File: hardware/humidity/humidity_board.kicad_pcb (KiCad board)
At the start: 2 copper layers, 21 parts, among them IC1 ATMEGA88-A, J1 RJ45, P1 ISP, P2 UART, SW1 SW_RESET, U1 ST485, U2 HYT271

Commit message: begin with humidity board pcb
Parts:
- moved U2 12.2 mm to (152.0, 149.0)
- moved J1 0.56 mm to (262.0, 149.0)
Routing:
- net GND: track 0.00 -> 29.6 mm
- net VCC: track 0.00 -> 3.14 mm
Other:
- net class Default: trace_width 0.254 -> 0.7; via_dia 0.889 -> 1.2; via_drill 0.635 -> 0.6
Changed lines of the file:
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@@
   (general
     (links 61)
-    (no_connects 61)
-    (area 0 0 0 0)
+    (no_connects 57)
+    (area 159.572 124.481 284.2884 167.38335)
     (thickness 1.6)
-    (drawings 0)
-    (tracks 0)
+    (drawings 1)
+    (tracks 11)
     (zones 0)
     (modules 21)
@@
   )
   (setup
-    (last_trace_width 0.254)
+    (last_trace_width 0.7)
     (trace_clearance 0.254)
     (zone_clearance 0.508)
@@
     (segment_width 0.2)
     (edge_width 0.1)
-    (via_size 0.889)
-    (via_drill 0.635)
+    (via_size 1.2)
+    (via_drill 0.6)
     (via_min_size 0.889)
     (via_min_drill 0.508)
@@
     (pad_to_mask_clearance 0)
     (aux_axis_origin 0 0)
-    (visible_elements FFFFFBBF)
+    (visible_elements FFFFFFBF)
     (pcbplotparams
       (layerselection 3178497)
@@
   (net_class Default "This is the default net class."
     (clearance 0.254)
-    (trace_width 0.254)
-    (via_dia 0.889)
-    (via_drill 0.635)
+    (trace_width 0.7)
+    (via_dia 1.2)
+    (via_drill 0.6)
     (uvia_dia 0.508)
     (uvia_drill 0.127)
@@
     (add_net VCC)
   )
+  (module RJ45_8P8_simple (layer F.Cu)
+    (at 262 149 270)
+    (tags RJ45)
+    (fp_text reference J1 (at 0 -21.5 270) (layer F.SilkS)
+      (effects (font (size 1.524 1.524) (thickness 0.3048)))
+    )
+    (fp_text value RJ45 (at 0.14224 -0.1016 270) (layer F.SilkS)
+      (effects (font (size 1.00076 1.00076) (thickness 0.2032)))
+    )
+    (fp_line (start 5.5 -20) (end 5.5 -9) (layer F.SilkS) (width 0.15))
+    (fp_line (start -5.5 -9) (end 5.5 -9) (layer F.SilkS) (width 0.15))
+    (fp_line (start -5.5 -20) (end -5.5 -9) (layer F.SilkS) (width 0.15))
+    (fp_line (start -8 -20) (end 8 -20) (layer F.SilkS) (width 0.15))
+    (fp_line (start 8 -20) (end 8 1.5) (layer F.SilkS) (width 0.15))
+    (fp_line (start 8 1.5) (end -8 1.5) (layer F.SilkS) (width 0.15))
+    (fp_line (start -8 1.5) (end -8 -20) (layer F.SilkS) (width 0.15))
+    (pad "" np_thru_hole circle (at -5.715 -8.9 90) (size 3.4 3.4) (drill 3.4)
+      (layers *.Cu *.SilkS *.Mask)
+    )
+    (pad "" np_thru_hole circle (at 5.715 -8.9 90) (size 3.4 3.4) (drill 3.4)
+      (layers *.Cu *.SilkS *.Mask)
+    )
+    (pad 1 thru_hole rect (at 4.445 -2.54 90) (size 1.9 1.9) (drill 0.8)
+      (layers *.Cu *.Mask F.SilkS)
+      (net 12 /za)
+    )
+    (pad 2 thru_hole circle (at 3.175 0 90) (size 1.9 1.9) (drill 0.8)
+      (layers *.Cu *.Mask F.SilkS)
+      (net 13 /zb)
+    )
+    (pad 3 thru_hole circle (at 1.905 -2.54 90) (size 1.9 1.9) (drill 0.8)
+      (layers *.Cu *.Mask F.SilkS)
+    )
+    (pad 4 thru_hole circle (at 0.63 0 90) (size 1.9 1.9) (drill 0.8)
+      (layers *.Cu *.Mask F.SilkS)
+      (net 18 VCC)
+    )
+    (pad 5 thru_hole circle (at -0.635 -2.54 90) (size 1.9 1.9) (drill 0.8)
+      (layers *.Cu *.Mask F.SilkS)
+      (net 18 VCC)
+    )
+    (pad 6 thru_hole circle (at -1.905 0 90) (size 1.9 1.9) (drill 0.8)
+      (layers *.Cu *.Mask F.SilkS)
+    )
+    (pad 7 thru_hole circle (at -3.175 -2.54 90) (size 1.9 1.9) (drill 0.8)
+      (layers *.Cu *.Mask F.SilkS)
+      (net 14 GND)
+    )
+    (pad 8 thru_hole circle (at -4.445 0 90) (size 1.9 1.9) (drill 0.8)
+      (layers *.Cu *.Mask F.SilkS)
+      (net 14 GND)
+    )
+    (pad 9 thru_hole circle (at 7.9 -12 90) (size 3 3) (drill 1.6)
+      (layers *.Cu *.Mask F.SilkS)
+      (net 14 GND)
+    )
+    (pad 9 thru_hole circle (at -7.9 -12 90) (size 3 3) (drill 1.6)
+      (layers *.Cu *.Mask F.SilkS)
+      (net 14 GND)
+    )
+    (model connectors/RJ45_8.wrl
+      (at (xyz 0 0 0))
+      (scale (xyz 0.4 0.4 0.4))
+      (rotate (xyz 0 0 0))
+    )
+  )
   (module wannenstecker_2x5_rm254 (layer F.Cu)
     (at 220.98 130.81)
@@
     )
   )
-  (module RJ45_8P8_simple (layer F.Cu)
-    (at 261.62 148.59 270)
-    (tags RJ45)
-    (fp_text reference J1 (at 0 -21.5 270) (layer F.SilkS)
-      (effects (font (size 1.524 1.524) (thickness 0.3048)))
-    )
-    (fp_text value RJ45 (at 0.14224 -0.1016 270) (layer F.SilkS)
-      (effects (font (size 1.00076 1.00076) (thickness 0.2032)))
-    )
-    (fp_line (start 5.5 -20) (end 5.5 -9) (layer F.SilkS) (width 0.15))
-    (fp_line (start -5.5 -9) (end 5.5 -9) (layer F.SilkS) (width 0.15))
-    (fp_line (start -5.5 -20) (end -5.5 -9) (layer F.SilkS) (width 0.15))
-    (fp_line (start -8 -20) (end 8 -20) (layer F.SilkS) (width 0.15))
-    (fp_line (start 8 -20) (end 8 1.5) (layer F.SilkS) (width 0.15))
-    (fp_line (start 8 1.5) (end -8 1.5) (layer F.SilkS) (width 0.15))
-    (fp_line (start -8 1.5) (end -8 -20) (layer F.SilkS) (width 0.15))
-    (pad "" np_thru_hole circle (at -5.715 -8.9 90) (size 3.4 3.4) (drill 3.4)
-      (layers *.Cu *.SilkS *.Mask)
-    )
-    (pad "" np_thru_hole circle (at 5.715 -8.9 90) (size 3.4 3.4) (drill 3.4)
-      (layers *.Cu *.SilkS *.Mask)
-    )
-    (pad 1 thru_hole rect (at 4.445 -2.54 90) (size 1.9 1.9) (drill 0.8)
-      (layers *.Cu *.Mask F.SilkS)
-      (net 12 /za)
-    )
-    (pad 2 thru_hole circle (at 3.175 0 90) (size 1.9 1.9) (drill 0.8)
-      (layers *.Cu *.Mask F.SilkS)
-      (net 13 /zb)
-    )
-    (pad 3 thru_hole circle (at 1.905 -2.54 90) (size 1.9 1.9) (drill 0.8)
-      (layers *.Cu *.Mask F.SilkS)
-    )
-    (pad 4 thru_hole circle (at 0.63 0 90) (size 1.9 1.9) (drill 0.8)
-      (layers *.Cu *.Mask F.SilkS)
-      (net 18 VCC)
-    )
-    (pad 5 thru_hole circle (at -0.635 -2.54 90) (size 1.9 1.9) (drill 0.8)
-      (layers *.Cu *.Mask F.SilkS)
-      (net 18 VCC)
-    )
-    (pad 6 thru_hole circle (at -1.905 0 90) (size 1.9 1.9) (drill 0.8)
-      (layers *.Cu *.Mask F.SilkS)
-    )
-    (pad 7 thru_hole circle (at -3.175 -2.54 90) (size 1.9 1.9) (drill 0.8)
-      (layers *.Cu *.Mask F.SilkS)
-      (net 14 GND)
-    )
-    (pad 8 thru_hole circle (at -4.445 0 90) (size 1.9 1.9) (drill 0.8)
-      (layers *.Cu *.Mask F.SilkS)
-      (net 14 GND)
-    )
-    (pad 9 thru_hole circle (at 7.9 -12 90) (size 3 3) (drill 1.6)
-      (layers *.Cu *.Mask F.SilkS)
-      (net 14 GND)
-    )
-    (pad 9 thru_hole circle (at -7.9 -12 90) (size 3 3) (drill 1.6)
-      (layers *.Cu *.Mask F.SilkS)
-      (net 14 GND)
-    )
-    (model connectors/RJ45_8.wrl
-      (at (xyz 0 0 0))
-      (scale (xyz 0.4 0.4 0.4))
-      (rotate (xyz 0 0 0))
-    )
-  )
   (module HYT271 (layer F.Cu)
-    (at 163.83 146.05 270)
+    (at 152 149 270)
     (fp_text reference U2 (at 0 3.429 270) (layer F.SilkS)
       (effects (font (size 1 1) (thickness 0.15)))
@@
     )
   )
+  (gr_line (start 308 149) (end 71 149) (angle 90) (layer Cmts.User) (width 0.2))
+  (segment (start 264.54 145.825) (end 266.175 145.825) (width 0.7) (layer F.Cu) (net 14) (status 400000))
+  (segment (start 269.35 149) (end 274 149) (width 0.7) (layer F.Cu) (net 14))
+  (segment (start 266.175 145.825) (end 269.35 149) (width 0.7) (layer F.Cu) (net 14))
+  (segment (start 262 144.555) (end 262.055 144.555) (width 0.7) (layer F.Cu) (net 14) (status C00000))
+  (segment (start 263.325 145.825) (end 264.54 145.825) (width 0.7) (layer F.Cu) (net 14) (status 800000))
+  (segment (start 262.055 144.555) (end 263.325 145.825) (width 0.7) (layer F.Cu) (net 14) (status 400000))
+  (segment (start 274 141.1) (end 274 149) (width 0.7) (layer F.Cu) (net 14) (status 400000))
+  (segment (start 274 149) (end 274 156.9) (width 0.7) (layer F.Cu) (net 14) (status 800000))
+  (segment (start 262 149.63) (end 262 149.5) (width 0.7) (layer F.Cu) (net 18) (status C00000))
+  (segment (start 263.135 148.365) (end 264.54 148.365) (width 0.7) (layer F.Cu) (net 18) (status 800000))
+  (segment (start 262 149.5) (end 263.135 148.365) (width 0.7) (layer F.Cu) (net 18) (status 400000))
 )

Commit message: add m3 schraube
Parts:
- added m3_loch: VAL**, m3_loch, F.Cu at (250.5, 155.0)
- added m3_loch: VAL**, m3_loch, F.Cu at (176.0, 140.0)
- moved R6 36.2 mm to (250.0, 146.5)
- moved C5 26.6 mm to (249.5, 150.0)
- moved U1 22.4 mm to (239.5, 149.5)
- moved P1 21.9 mm to (200.5, 138.5)
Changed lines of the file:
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@@
     (tracks 11)
     (zones 0)
-    (modules 21)
+    (modules 23)
     (nets 19)
   )
@@
   )
   (module wannenstecker_2x5_rm254 (layer F.Cu)
-    (at 220.98 130.81)
+    (at 200.5 138.5)
     (fp_text reference P1 (at 0 -5.5) (layer F.SilkS)
       (effects (font (size 1 1) (thickness 0.15)))
@@
   )
   (module st485 (layer F.Cu)
-    (at 217.17 151.13)
+    (at 239.5 149.5)
     (descr st485)
     (attr smd)
@@
   )
   (module SM0603_big (layer F.Cu)
-    (at 226.06 162.56)
+    (at 249.5 150)
     (tags "SM0603 R")
     (attr smd)
@@
   )
   (module SM0603_big (layer F.Cu)
-    (at 219.71 166.37)
+    (at 250 146.5)
     (tags "SM0603 R")
     (attr smd)
@@
     )
   )
+  (module m3_loch (layer F.Cu)
+    (at 250.5 155)
+    (fp_text reference m3_loch (at 0 -5.588) (layer F.SilkS)
+      (effects (font (size 1 1) (thickness 0.15)))
+    )
+    (fp_text value VAL** (at 0 5.842) (layer F.SilkS)
+      (effects (font (size 1 1) (thickness 0.15)))
+    )
+    (pad "" np_thru_hole circle (at 0 0) (size 3.4 3.4) (drill 3.4)
+      (layers *.Cu *.Mask F.SilkS)
+      (clearance 3.3)
+    )
+  )
+  (module m3_loch (layer F.Cu)
+    (at 176 140)
+    (fp_text reference m3_loch (at 0 -5.588) (layer F.SilkS)
+      (effects (font (size 1 1) (thickness 0.15)))
+    )
+    (fp_text value VAL** (at 0 5.842) (layer F.SilkS)
+      (effects (font (size 1 1) (thickness 0.15)))
+    )
+    (pad "" np_thru_hole circle (at 0 0) (size 3.4 3.4) (drill 3.4)
+      (layers *.Cu *.Mask F.SilkS)
+      (clearance 3.3)
+    )
+  )
   (gr_line (start 308 149) (end 71 149) (angle 90) (layer Cmts.User) (width 0.2))
-  (segment (start 264.54 145.825) (end 266.175 145.825) (width 0.7) (layer F.Cu) (net 14) (status 400000))
+  (segment (start 264.54 145.825) (end 266.175 145.825) (width 0.7) (layer F.Cu) (net 14))
   (segment (start 269.35 149) (end 274 149) (width 0.7) (layer F.Cu) (net 14))
   (segment (start 266.175 145.825) (end 269.35 149) (width 0.7) (layer F.Cu) (net 14))
-  (segment (start 262 144.555) (end 262.055 144.555) (width 0.7) (layer F.Cu) (net 14) (status C00000))
-  (segment (start 263.325 145.825) (end 264.54 145.825) (width 0.7) (layer F.Cu) (net 14) (status 800000))
-  (segment (start 262.055 144.555) (end 263.325 145.825) (width 0.7) (layer F.Cu) (net 14) (status 400000))
-  (segment (start 274 141.1) (end 274 149) (width 0.7) (layer F.Cu) (net 14) (status 400000))
-  (segment (start 274 149) (end 274 156.9) (width 0.7) (layer F.Cu) (net 14) (status 800000))
-  (segment (start 262 149.63) (end 262 149.5) (width 0.7) (layer F.Cu) (net 18) (status C00000))
-  (segment (start 263.135 148.365) (end 264.54 148.365) (width 0.7) (layer F.Cu) (net 18) (status 800000))
-  (segment (start 262 149.5) (end 263.135 148.365) (width 0.7) (layer F.Cu) (net 18) (status 400000))
+  (segment (start 262 144.555) (end 262.055 144.555) (width 0.7) (layer F.Cu) (net 14))
+  (segment (start 263.325 145.825) (end 264.54 145.825) (width 0.7) (layer F.Cu) (net 14))
+  (segment (start 262.055 144.555) (end 263.325 145.825) (width 0.7) (layer F.Cu) (net 14))
+  (segment (start 274 141.1) (end 274 149) (width 0.7) (layer F.Cu) (net 14))
+  (segment (start 274 149) (end 274 156.9) (width 0.7) (layer F.Cu) (net 14))
+  (segment (start 262 149.63) (end 262 149.5) (width 0.7) (layer F.Cu) (net 18))
+  (segment (start 263.135 148.365) (end 264.54 148.365) (width 0.7) (layer F.Cu) (net 18))
+  (segment (start 262 149.5) (end 263.135 148.365) (width 0.7) (layer F.Cu) (net 18))
 )

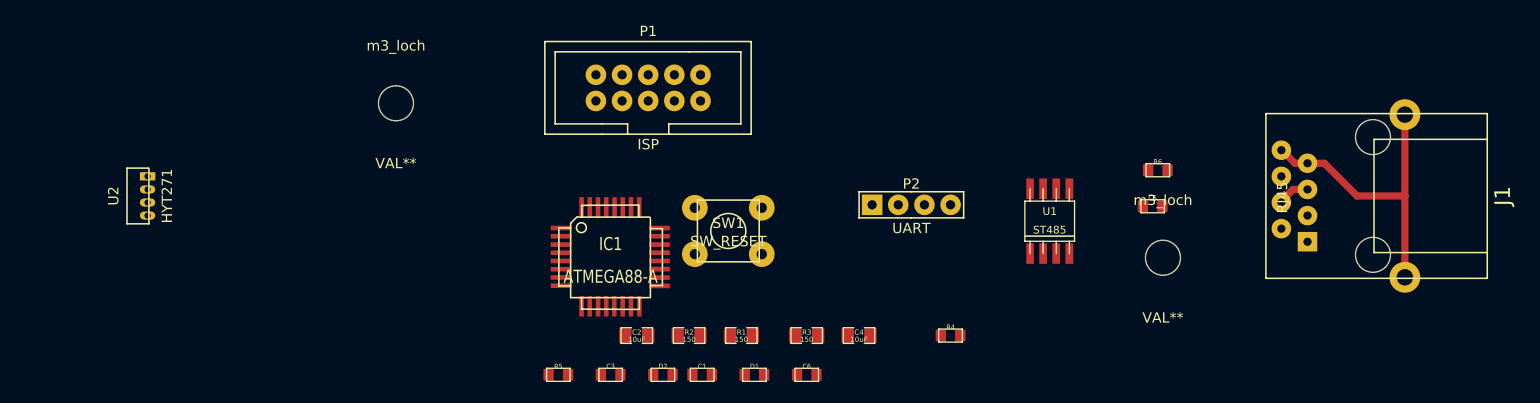
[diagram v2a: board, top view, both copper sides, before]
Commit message: humidity pcb finished
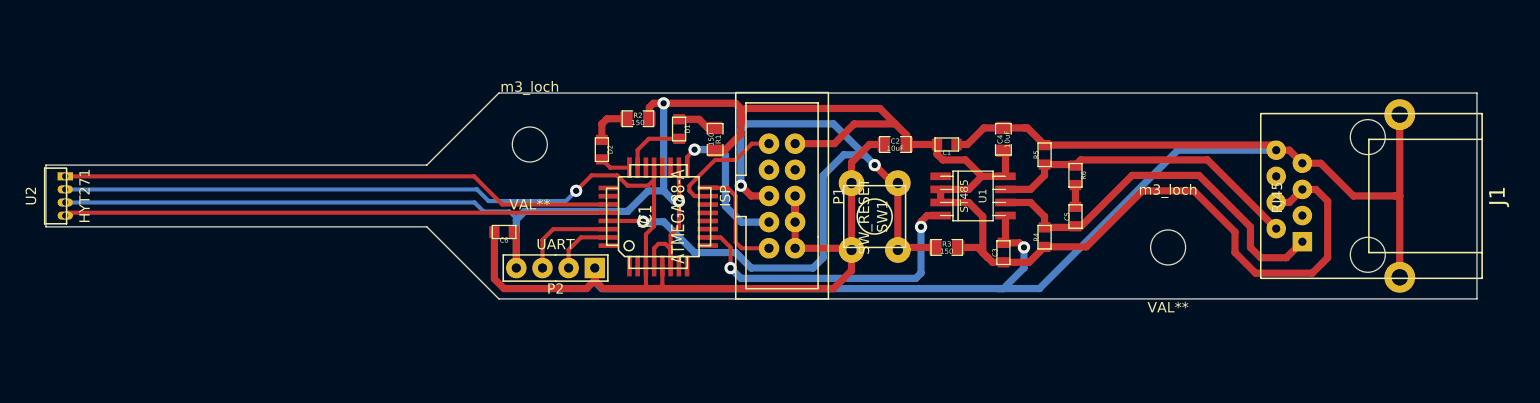
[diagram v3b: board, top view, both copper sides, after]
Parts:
- moved R5 51.8 mm to (239.0, 145.0), turned to 90 degrees
- moved C3 40.0 mm to (235.0, 154.5), turned to 90 degrees
- moved P2 35.1 mm to (191.5, 156.0), turned to 180 degrees
- moved C1 32.6 mm to (229.5, 144.0), turned to 180 degrees
- moved C6 32.5 mm to (186.5, 152.5), turned to 180 degrees
- moved C2 31.2 mm to (224.5, 144.0)
- moved D1 25.0 mm to (203.5, 142.5), turned to 270 degrees
- moved C4 23.7 mm to (235.0, 143.5), turned to 90 degrees
- moved D2 22.7 mm to (196.0, 144.5), turned to 270 degrees
- moved R2 21.6 mm to (199.5, 141.5)
- moved R1 19.2 mm to (207.0, 143.5), turned to 270 degrees
- moved P1 16.7 mm to (213.5, 149.0), turned to 270 degrees
- moved R3 16.1 mm to (229.5, 154.0)
- moved SW1 14.3 mm to (222.5, 151.0), turned to 270 degrees
- moved m3_loch 13.6 mm to (189.0, 144.0)
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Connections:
- R6 pad 1: (no net) -> /zb
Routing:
- net GND: track 29.6 -> 299.7 mm, vias 0 -> 2
- net VCC: track 3.14 -> 229.6 mm, vias 0 -> 2
- net /RESET: track 0.00 -> 72.7 mm, vias 0 -> 3
- net /SDA: track 0.00 -> 53.9 mm
- net /SCL: track 0.00 -> 52.9 mm
- net /za: track 0.00 -> 37.7 mm
- net /zb: track 0.00 -> 31.0 mm
- net /DI: track 0.00 -> 30.9 mm, vias 0 -> 2
- net /SCK: track 0.00 -> 15.1 mm, vias 0 -> 1
- net /MOSI: track 0.00 -> 11.9 mm
- net /MISO: track 0.00 -> 11.0 mm
- net /RX: track 0.00 -> 9.61 mm
- net /LED1: track 0.00 -> 6.20 mm
- net /TX: track 0.00 -> 6.17 mm
- net N-0000015: track 0.00 -> 4.15 mm
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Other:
- board outline added: 139 x 20 mm
- net class uc added: clearance 0.254, trace_width 0.4, via_dia 1.2, via_drill 0.6

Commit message: checking
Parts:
- removed the m3_loch at (251.0, 154.0)
- removed the m3_loch at (189.0, 144.0)
- added m3_loch: VAL**, m3_loch, F.Cu at (187.5, 101.0)
- added m3_loch: VAL**, m3_loch, F.Cu at (125.5, 91.0)
- moved C1 82.7 mm to (166.0, 91.0)
- moved C2 82.7 mm to (161.0, 91.0)
- moved C3 82.7 mm to (171.5, 101.5)
- moved C4 82.7 mm to (171.5, 90.5)
- moved C5 82.7 mm to (178.5, 98.0)
- moved C6 82.7 mm to (123.0, 99.5)
- moved D1 82.7 mm to (140.0, 89.5)
- moved D2 82.7 mm to (132.5, 91.5)
- moved IC1 82.7 mm to (138.0, 98.0)
- moved J1 82.7 mm to (198.0, 96.0)
- moved P1 82.7 mm to (150.0, 96.0)
- moved P2 82.7 mm to (128.0, 103.0)
- moved R1 82.7 mm to (143.5, 90.5)
- moved R2 82.7 mm to (136.0, 88.5)
- moved R3 82.7 mm to (166.0, 101.0)
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
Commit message: TODO change sensor module
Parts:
- moved C1 26.3 mm to (143.1, 104.0), turned to 90 degrees
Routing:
- net VCC: track 229.6 -> 235.8 mm
- net GND: track 299.7 -> 294.4 mm
- added copper zone on B.Cu, net GND
- added copper zone on F.Cu, net GND
